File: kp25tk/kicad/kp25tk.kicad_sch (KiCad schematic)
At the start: 74 parts, among them J1 Host Connector, J2 Config Header, J3 Power In, J4 Row Select In, J5 Column Out, J6 NMI Out, J7 Reset Out, J8 Switch, SW0 KEY00, SW1 KEY01, SW10 KEY0A, SW11 KEY0B, SW12 KEY0C, SW13 KEY0D, SW14 KEY0E, SW15 KEY0F, SW16 KEY10, SW17 KEY11, SW18 KEY12, SW19 KEY13, SW2 KEY02, SW20 KEY14, SW21 KEY15, SW22 KEY16, SW23 KEY17, SW24 NMI, SW25 RESET, SW27 SWITCH, SW3 KEY03, SW4 KEY04, SW5 KEY05, SW6 KEY06, SW7 KEY07, SW8 KEY08, SW9 KEY09, U1 74LS14

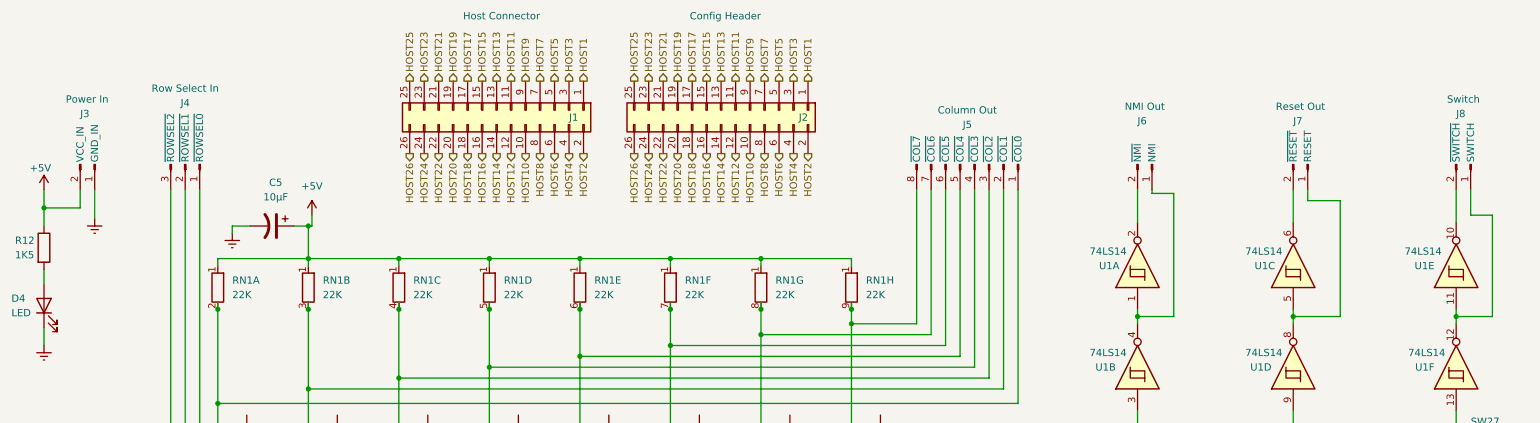
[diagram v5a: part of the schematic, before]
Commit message: kp25tk/: Add SWLED to indicate when switch is on/up
We change the pull-up for the power LED from R12 to R4, so it matches
the diode number D4, and change the value to D4 to "PWR." (It's not
clear to me that this is the correct attribute to change to name the
LED "PWR," though.)

We add LED D5 and pull-up R5 driving it, pulled down by /SWITCH
(negative logic output of slide switch buffers) to light it when the
switch is on.

README is updated with the design notes for this, and also a new
component summary (only partially complete) which serves as a rough
guide to the reference numbering we're using on components.
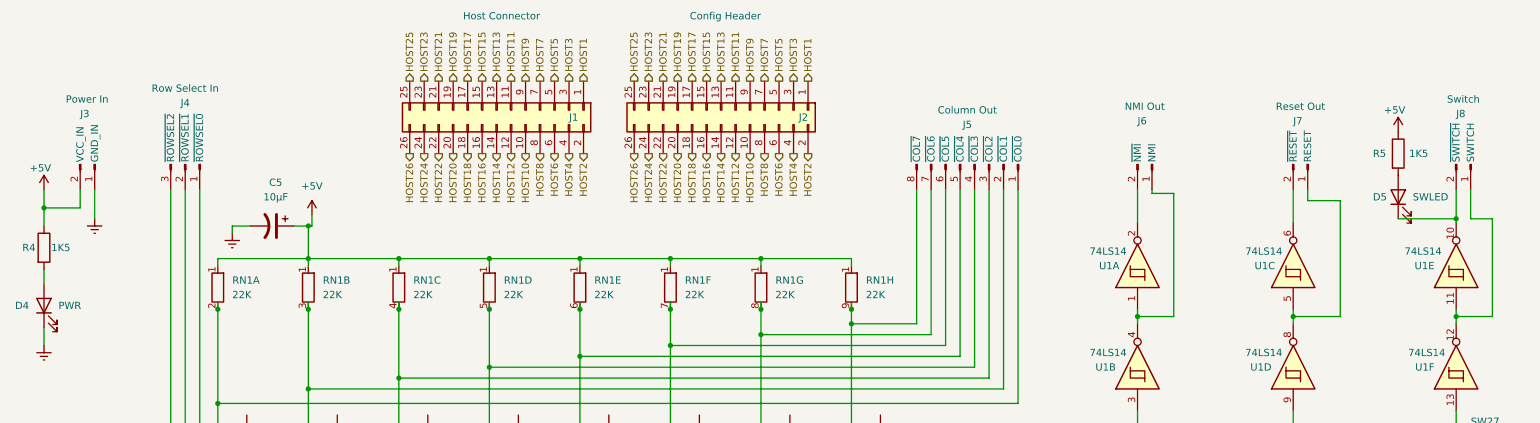
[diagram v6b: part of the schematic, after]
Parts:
- added D5: SWLED, LED_THT:LED_D3.0mm, symbol Device:LED
- added R5: 1K5, Resistor_THT:R_Axial_DIN0207_L6.3mm_D2.5mm_P10.16mm_Horizontal, symbol Device:R
- D4: value LED -> PWR
- renumbered R12 to R4
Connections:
- net +5V: now also R5.1
- net at J8.2 (~{SWITCH}), U1.10: now also D5.1 (K)
- new net: D5.2 (A), R5.2
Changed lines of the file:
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@@
   (junction (at 69.215 62.865) (diameter 0) (color 0 0 0 0)
   )
+  (junction (at 270.51 55.88) (diameter 0) (color 0 0 0 0)
+  )
   (junction (at 158.75 130.175) (diameter 0) (color 0 0 0 0)
   )
@@
     (stroke (width 0) (type default))
   )
-  (wire (pts (xy 273.05 50.8) (xy 273.05 55.245))
+  (wire (pts (xy 273.05 50.8) (xy 273.05 55.88))
     (stroke (width 0) (type default))
   )
@@
     (stroke (width 0) (type default))
   )
-  (wire (pts (xy 276.86 55.245) (xy 276.86 73.025))
+  (wire (pts (xy 276.86 55.88) (xy 276.86 73.025))
     (stroke (width 0) (type default))
   )
@@
     (stroke (width 0) (type default))
   )
+  (wire (pts (xy 260.35 55.88) (xy 270.51 55.88))
+    (stroke (width 0) (type default))
+  )
   (wire (pts (xy 85.09 71.755) (xy 85.09 83.82))
     (stroke (width 0) (type default))
@@
     (stroke (width 0) (type default))
   )
+  (wire (pts (xy 270.51 55.88) (xy 270.51 56.515))
+    (stroke (width 0) (type default))
+  )
   (wire (pts (xy 55.88 57.15) (xy 59.055 57.15))
     (stroke (width 0) (type default))
@@
     (stroke (width 0) (type default))
   )
-  (wire (pts (xy 270.51 50.8) (xy 270.51 56.515))
+  (wire (pts (xy 270.51 50.8) (xy 270.51 55.88))
     (stroke (width 0) (type default))
   )
@@
     (stroke (width 0) (type default))
   )
-  (wire (pts (xy 273.05 55.245) (xy 276.86 55.245))
+  (wire (pts (xy 273.05 55.88) (xy 276.86 55.88))
     (stroke (width 0) (type default))
   )
@@
   (symbol (lib_id "Device:LED") (at 22.86 71.12 90) (unit 1)
     (in_bom yes) (on_board yes) (dnp no)
-    (property "Reference" "D4" (at 17.145 69.85 90)
+    (property "Reference" "D4" (at 17.78 71.12 90)
       (effects (font (size 1.27 1.27)) (justify right))
     )
-    (property "Value" "LED" (at 17.145 72.39 90)
+    (property "Value" "PWR" (at 25.4 71.12 90)
       (effects (font (size 1.27 1.27)) (justify right))
     )
@@
     )
   )
+  (symbol (lib_id "Device:R") (at 260.35 44.45 0) (unit 1)
+    (in_bom yes) (on_board yes) (dnp no)
+    (property "Reference" "R5" (at 255.905 44.45 0)
+      (effects (font (size 1.27 1.27)) (justify left))
+    )
+    (property "Value" "1K5" (at 262.255 44.45 0)
+      (effects (font (size 1.27 1.27)) (justify left))
+    )
+    (property "Footprint" "Resistor_THT:R_Axial_DIN0207_L6.3mm_D2.5mm_P10.16mm_Horizontal" (at 258.572 44.45 90)
+      (effects (font (size 1.27 1.27)) hide)
+    )
+    (property "Datasheet" "~" (at 260.35 44.45 0)
+      (effects (font (size 1.27 1.27)) hide)
+    )
+    (pin "1")
+    (pin "2")
+    (instances
+      (project "kp25tk"
+        (path "/599b5491-557a-4ec9-bd4a-925136423376"
+          (reference "R5") (unit 1)
+        )
+      )
+    )
+  )
   (symbol (lib_id "Switch:SW_Push") (at 90.17 107.315 0) (unit 1)
     (in_bom yes) (on_board yes) (dnp no)
@@
     )
   )
+  (symbol (lib_id "power:+5V") (at 260.35 40.64 0) (unit 1)
+    (in_bom yes) (on_board yes) (dnp no)
+    (property "Reference" "#PWR014" (at 260.35 44.45 0)
+      (effects (font (size 1.27 1.27)) hide)
+    )
+    (property "Value" "+5V" (at 259.715 36.83 0)
+      (effects (font (size 1.27 1.27)))
+    )
+    (property "Footprint" "" (at 260.35 40.64 0)
+      (effects (font (size 1.27 1.27)) hide)
+    )
+    (property "Datasheet" "" (at 260.35 40.64 0)
+      (effects (font (size 1.27 1.27)) hide)
+    )
+    (pin "1")
+    (instances
+      (project "kp25tk"
+        (path "/599b5491-557a-4ec9-bd4a-925136423376"
+          (reference "#PWR014") (unit 1)
+        )
+      )
+    )
+  )
   (symbol (lib_id "Switch:SW_Push") (at 121.92 93.345 0) (unit 1)
     (in_bom yes) (on_board yes) (dnp no)
@@
     )
   )
+  (symbol (lib_id "Device:LED") (at 260.35 52.07 90) (unit 1)
+    (in_bom yes) (on_board yes) (dnp no)
+    (property "Reference" "D5" (at 255.905 52.07 90)
+      (effects (font (size 1.27 1.27)) (justify right))
+    )
+    (property "Value" "SWLED" (at 262.89 52.07 90)
+      (effects (font (size 1.27 1.27)) (justify right))
+    )
+    (property "Footprint" "LED_THT:LED_D3.0mm" (at 260.35 52.07 0)
+      (effects (font (size 1.27 1.27)) hide)
+    )
+    (property "Datasheet" "~" (at 260.35 52.07 0)
+      (effects (font (size 1.27 1.27)) hide)
+    )
+    (pin "1")
+    (pin "2")
+    (instances
+      (project "kp25tk"
+        (path "/599b5491-557a-4ec9-bd4a-925136423376"
+          (reference "D5") (unit 1)
+        )
+      )
+    )
+  )
   (symbol (lib_id "Diode:1N4148") (at 111.125 97.79 90) (unit 1)
     (in_bom yes) (on_board yes) (dnp no)
@@
   (symbol (lib_id "Device:R") (at 22.86 60.96 0) (unit 1)
     (in_bom yes) (on_board yes) (dnp no)
-    (property "Reference" "R12" (at 17.78 59.69 0)
+    (property "Reference" "R4" (at 19.05 60.96 0)
       (effects (font (size 1.27 1.27)) (justify left))
     )
-    (property "Value" "1K5" (at 17.78 62.23 0)
+    (property "Value" "1K5" (at 24.13 60.96 0)
       (effects (font (size 1.27 1.27)) (justify left))
     )
@@
       (project "kp25tk"
         (path "/599b5491-557a-4ec9-bd4a-925136423376"
-          (reference "R12") (unit 1)
+          (reference "R4") (unit 1)
         )
       )
